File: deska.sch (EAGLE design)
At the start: 18 parts, among them Q1 BC547, Q2 BC547

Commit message: +
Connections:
- net +5V: now also TIN-2.KL, TOUT-2.KL, TUT-2.KL; no longer TIN-1.KL, TOUT-1.KL, TUT-1.KL
- net GND: now also TIN-1.KL, TOUT-1.KL, TUT-1.KL; no longer TIN-3.KL, TOUT-3.KL, TUT-3.KL
- net N$1: now also TIN-3.KL; no longer TIN-2.KL
- net N$19: now also TOUT-3.KL; no longer TOUT-2.KL
- net N$3: now also TUT-3.KL; no longer TUT-2.KL
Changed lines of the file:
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@@
 <wire x1="33.02" y1="60.96" x2="20.32" y2="60.96" width="0.1524" layer="91"/>
 <wire x1="20.32" y1="60.96" x2="12.7" y2="60.96" width="0.1524" layer="91"/>
-<wire x1="12.7" y1="91.44" x2="12.7" y2="60.96" width="0.1524" layer="91"/>
 <pinref part="R1" gate="G$1" pin="1"/>
+<wire x1="12.7" y1="88.9" x2="12.7" y2="60.96" width="0.1524" layer="91"/>
 <wire x1="20.32" y1="63.5" x2="20.32" y2="60.96" width="0.1524" layer="91"/>
 <junction x="20.32" y="60.96"/>
-<pinref part="TIN" gate="-2" pin="KL"/>
-<wire x1="-2.54" y1="91.44" x2="12.7" y2="91.44" width="0.1524" layer="91"/>
 <pinref part="WEMOS1" gate="D1" pin="D0"/>
 <wire x1="48.26" y1="66.04" x2="33.02" y2="66.04" width="0.1524" layer="91"/>
 <wire x1="33.02" y1="66.04" x2="33.02" y2="60.96" width="0.1524" layer="91"/>
+<pinref part="TIN" gate="-3" pin="KL"/>
+<wire x1="-2.54" y1="88.9" x2="12.7" y2="88.9" width="0.1524" layer="91"/>
 </segment>
 </net>
@@
 <segment>
 <wire x1="38.1" y1="53.34" x2="15.24" y2="53.34" width="0.1524" layer="91"/>
-<pinref part="TUT" gate="-2" pin="KL"/>
 <wire x1="15.24" y1="53.34" x2="7.62" y2="53.34" width="0.1524" layer="91"/>
-<wire x1="-2.54" y1="60.96" x2="7.62" y2="60.96" width="0.1524" layer="91"/>
-<wire x1="7.62" y1="60.96" x2="7.62" y2="53.34" width="0.1524" layer="91"/>
 <pinref part="R3" gate="G$1" pin="1"/>
+<wire x1="7.62" y1="58.42" x2="7.62" y2="53.34" width="0.1524" layer="91"/>
 <wire x1="15.24" y1="63.5" x2="15.24" y2="53.34" width="0.1524" layer="91"/>
 <junction x="15.24" y="53.34"/>
@@
 <wire x1="48.26" y1="60.96" x2="38.1" y2="60.96" width="0.1524" layer="91"/>
 <wire x1="38.1" y1="60.96" x2="38.1" y2="53.34" width="0.1524" layer="91"/>
+<pinref part="TUT" gate="-3" pin="KL"/>
+<wire x1="-2.54" y1="58.42" x2="7.62" y2="58.42" width="0.1524" layer="91"/>
 </segment>
 </net>
@@
 </segment>
 <segment>
-<wire x1="0" y1="73.66" x2="0" y2="58.42" width="0.1524" layer="91"/>
-<pinref part="TOUT" gate="-3" pin="KL"/>
-<wire x1="0" y1="58.42" x2="0" y2="53.34" width="0.1524" layer="91"/>
-<wire x1="-2.54" y1="73.66" x2="0" y2="73.66" width="0.1524" layer="91"/>
-<pinref part="GND5" gate="1" pin="GND"/>
-<pinref part="TUT" gate="-3" pin="KL"/>
-<wire x1="-2.54" y1="58.42" x2="0" y2="58.42" width="0.1524" layer="91"/>
-<junction x="0" y="58.42"/>
-<wire x1="0" y1="73.66" x2="0" y2="88.9" width="0.1524" layer="91"/>
-<junction x="0" y="73.66"/>
-<pinref part="TIN" gate="-3" pin="KL"/>
-<wire x1="0" y1="88.9" x2="-2.54" y2="88.9" width="0.1524" layer="91"/>
-</segment>
-<segment>
 <pinref part="NAPAJENI" gate="-2" pin="KL"/>
 <pinref part="GND6" gate="1" pin="GND"/>
+</segment>
+<segment>
+<pinref part="GND5" gate="1" pin="GND"/>
+<wire x1="0" y1="91.44" x2="0" y2="78.74" width="0.1524" layer="91"/>
+<wire x1="0" y1="78.74" x2="0" y2="76.2" width="0.1524" layer="91"/>
+<wire x1="0" y1="76.2" x2="0" y2="63.5" width="0.1524" layer="91"/>
+<wire x1="0" y1="63.5" x2="0" y2="60.96" width="0.1524" layer="91"/>
+<wire x1="0" y1="60.96" x2="0" y2="53.34" width="0.1524" layer="91"/>
+<pinref part="TIN" gate="-1" pin="KL"/>
+<wire x1="-2.54" y1="93.98" x2="0" y2="93.98" width="0.1524" layer="91"/>
+<wire x1="0" y1="93.98" x2="0" y2="91.44" width="0.1524" layer="91"/>
+<pinref part="TOUT" gate="-1" pin="KL"/>
+<wire x1="-2.54" y1="78.74" x2="0" y2="78.74" width="0.1524" layer="91"/>
+<junction x="0" y="78.74"/>
+<pinref part="TUT" gate="-1" pin="KL"/>
+<wire x1="-2.54" y1="63.5" x2="0" y2="63.5" width="0.1524" layer="91"/>
+<junction x="0" y="63.5"/>
 </segment>
 </net>
@@
 <junction x="20.32" y="73.66"/>
 <wire x1="25.4" y1="93.98" x2="25.4" y2="73.66" width="0.1524" layer="91"/>
-<pinref part="TIN" gate="-1" pin="KL"/>
-<wire x1="-2.54" y1="93.98" x2="2.54" y2="93.98" width="0.1524" layer="91"/>
-<wire x1="2.54" y1="63.5" x2="2.54" y2="78.74" width="0.1524" layer="91"/>
-<pinref part="TUT" gate="-1" pin="KL"/>
-<wire x1="2.54" y1="78.74" x2="2.54" y2="93.98" width="0.1524" layer="91"/>
-<wire x1="-2.54" y1="63.5" x2="2.54" y2="63.5" width="0.1524" layer="91"/>
 <wire x1="2.54" y1="93.98" x2="17.78" y2="93.98" width="0.1524" layer="91"/>
-<junction x="2.54" y="93.98"/>
-<pinref part="TOUT" gate="-1" pin="KL"/>
 <wire x1="17.78" y1="93.98" x2="25.4" y2="93.98" width="0.1524" layer="91"/>
-<wire x1="-2.54" y1="78.74" x2="2.54" y2="78.74" width="0.1524" layer="91"/>
-<junction x="2.54" y="78.74"/>
 <wire x1="20.32" y1="73.66" x2="25.4" y2="73.66" width="0.1524" layer="91"/>
 <pinref part="P+2" gate="1" pin="+5V"/>
 <wire x1="17.78" y1="99.06" x2="17.78" y2="93.98" width="0.1524" layer="91"/>
 <junction x="17.78" y="93.98"/>
+<pinref part="TIN" gate="-2" pin="KL"/>
+<wire x1="-2.54" y1="91.44" x2="2.54" y2="91.44" width="0.1524" layer="91"/>
+<wire x1="2.54" y1="91.44" x2="2.54" y2="93.98" width="0.1524" layer="91"/>
+<pinref part="TOUT" gate="-2" pin="KL"/>
+<wire x1="-2.54" y1="76.2" x2="2.54" y2="76.2" width="0.1524" layer="91"/>
+<wire x1="2.54" y1="76.2" x2="2.54" y2="91.44" width="0.1524" layer="91"/>
+<junction x="2.54" y="91.44"/>
+<pinref part="TUT" gate="-2" pin="KL"/>
+<wire x1="-2.54" y1="60.96" x2="2.54" y2="60.96" width="0.1524" layer="91"/>
+<wire x1="2.54" y1="60.96" x2="2.54" y2="76.2" width="0.1524" layer="91"/>
+<junction x="2.54" y="76.2"/>
 </segment>
 <segment>
@@
 <junction x="17.78" y="55.88"/>
 <wire x1="17.78" y1="55.88" x2="10.16" y2="55.88" width="0.1524" layer="91"/>
-<pinref part="TOUT" gate="-2" pin="KL"/>
-<wire x1="-2.54" y1="76.2" x2="10.16" y2="76.2" width="0.1524" layer="91"/>
-<wire x1="10.16" y1="76.2" x2="10.16" y2="55.88" width="0.1524" layer="91"/>
 <pinref part="WEMOS1" gate="D1" pin="D5"/>
+<wire x1="10.16" y1="73.66" x2="10.16" y2="55.88" width="0.1524" layer="91"/>
 <wire x1="48.26" y1="63.5" x2="35.56" y2="63.5" width="0.1524" layer="91"/>
 <wire x1="35.56" y1="63.5" x2="35.56" y2="55.88" width="0.1524" layer="91"/>
-</segment>
-</net>
+<pinref part="TOUT" gate="-3" pin="KL"/>
+<wire x1="-2.54" y1="73.66" x2="10.16" y2="73.66" width="0.1524" layer="91"/>
+</segment>
+</net>

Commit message: upravy desky
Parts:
- removed BUZZER, LED, NAPAJENI, RELAY: (no value), con-wago-508:W237-02P
- removed I2CDISP, I2CKEYB: (no value), con-wago-508:W237-04P
- removed Q1, Q2: BC547, transistor-npn:BC547
- removed R5, R6: 1k, rcl:R-EU_0207/7
- removed TIN, TOUT, TUT: (no value), con-wago-508:W237-3E
- added DS18B1, DS18B2, DS18B20, LED+RELAY: (no value), con-wago-508:W237-03P
- added PIR, SERIAL: (no value), con-amp-quick:M03
- added SL1: (no value), con-amp-quick:M04
- added SOURCE: (no value), con-wago-508:W237-02P
- R1, R3: device rcl:R-EU_0207/7 -> rcl:R-EU_0207/10
- R2: value 4k7 -> 220; device rcl:R-EU_0207/7 -> rcl:R-EU_0207/10
- R4: value 220 -> 4k7; device rcl:R-EU_0207/7 -> rcl:R-EU_0207/10
- WEMOS1: device wemos:WEMOS-D1-MINI -> esp8266modules:WEMOS-D1-MINI
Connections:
- removed net N$12: I2CDISP-3.KL, I2CKEYB-3.KL, WEMOS1.D4
- removed net N$14: Q2.C, RELAY-1.KL
- removed net N$15: BUZZER-1.KL, Q1.C
- removed net N$16: R6.2, WEMOS1.D2
- removed net N$19: R2.1, TOUT-3.KL, WEMOS1.D5
- new net N$2: SERIAL.3, WEMOS1.RX
- new net N$8: LED+RELAY-3.KL, R2.2
- new net N$9: DS18B20-2.KL, R1.2, WEMOS1.D7
- net +5V: now also DS18B1-3.KL, DS18B2-3.KL, DS18B20-3.KL, LED+RELAY-2.KL, PIR.3, R1.1, R3.1, R4.1, SL1.2, SOURCE-1.KL; no longer I2CDISP-2.KL, I2CKEYB-2.KL, LED-2.KL, NAPAJENI-1.KL, R1.2, R2.2, R3.2, RELAY-2.KL, TIN-2.KL, TOUT-2.KL, TUT-2.KL
- net GND: now also DS18B1-1.KL, DS18B2-1.KL, DS18B20-1.KL, PIR.1, SERIAL.1, SL1.1, SOURCE-2.KL; no longer BUZZER-2.KL, I2CDISP-1.KL, I2CKEYB-1.KL, NAPAJENI-2.KL, Q1.E, Q2.E, TIN-1.KL, TOUT-1.KL, TUT-1.KL
- net N$1: now also SERIAL.2, WEMOS1.TX; no longer R1.1, TIN-3.KL, WEMOS1.D0
- net N$11: now also DS18B2-2.KL, R4.2, WEMOS1.D5; no longer I2CDISP-4.KL, I2CKEYB-4.KL, WEMOS1.D3
- net N$13: now also DS18B1-2.KL, R3.2, WEMOS1.D6; no longer Q2.B, R5.2
- net N$3: now also SL1.4, WEMOS1.D1; no longer R3.1, TUT-3.KL, WEMOS1.D6
- net N$4: now also SL1.3, WEMOS1.D2; no longer R5.1, WEMOS1.D7
- net N$5: now also PIR.2, WEMOS1.D0; no longer R4.1, WEMOS1.D8
- net N$6: now also R2.1, WEMOS1.D4; no longer LED-1.KL, R4.2
- net N$7: now also LED+RELAY-1.KL, WEMOS1.D3; no longer Q1.B, R6.1
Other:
- moved on the sheet: R1, R2, R3, R4, WEMOS1

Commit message: +
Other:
- moved on the sheet: R4
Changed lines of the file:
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@@
 <attribute name="VALUE" x="16.51" y="64.262" size="1.778" layer="96" rot="R180"/>
 </instance>
-<instance part="R4" gate="G$1" x="-12.7" y="63.5" smashed="yes" rot="R180">
-<attribute name="NAME" x="-8.89" y="62.0014" size="1.778" layer="95" rot="R180"/>
-<attribute name="VALUE" x="-8.89" y="66.802" size="1.778" layer="96" rot="R180"/>
+<instance part="R4" gate="G$1" x="-10.16" y="63.5" smashed="yes" rot="R180">
+<attribute name="NAME" x="-6.35" y="62.0014" size="1.778" layer="95" rot="R180"/>
+<attribute name="VALUE" x="-6.35" y="66.802" size="1.778" layer="96" rot="R180"/>
 </instance>
 <instance part="SOURCE" gate="-1" x="17.78" y="15.24" smashed="yes">
@@
 <pinref part="DS18B20" gate="-1" pin="KL"/>
 <pinref part="GND4" gate="1" pin="GND"/>
+<pinref part="DS18B1" gate="-1" pin="KL"/>
+<wire x1="5.08" y1="50.8" x2="27.94" y2="50.8" width="0.1524" layer="91"/>
+<junction x="27.94" y="50.8"/>
 <pinref part="DS18B2" gate="-1" pin="KL"/>
-<pinref part="DS18B1" gate="-1" pin="KL"/>
 <wire x1="-17.78" y1="50.8" x2="5.08" y2="50.8" width="0.1524" layer="91"/>
-<wire x1="5.08" y1="50.8" x2="27.94" y2="50.8" width="0.1524" layer="91"/>
 <junction x="5.08" y="50.8"/>
-<junction x="27.94" y="50.8"/>
 </segment>
 <segment>
@@
 <pinref part="R3" gate="G$1" pin="1"/>
 <wire x1="17.78" y1="45.72" x2="27.94" y2="45.72" width="0.1524" layer="91"/>
-<wire x1="-7.62" y1="63.5" x2="17.78" y2="63.5" width="0.1524" layer="91"/>
+<wire x1="-5.08" y1="63.5" x2="17.78" y2="63.5" width="0.1524" layer="91"/>
 <wire x1="17.78" y1="63.5" x2="17.78" y2="60.96" width="0.1524" layer="91"/>
 <wire x1="17.78" y1="60.96" x2="17.78" y2="45.72" width="0.1524" layer="91"/>
@@
 <wire x1="40.64" y1="58.42" x2="0" y2="58.42" width="0.1524" layer="91"/>
 <wire x1="0" y1="58.42" x2="0" y2="55.88" width="0.1524" layer="91"/>
+<pinref part="R4" gate="G$1" pin="2"/>
+<wire x1="-15.24" y1="55.88" x2="-15.24" y2="63.5" width="0.1524" layer="91"/>
+<wire x1="0" y1="55.88" x2="-15.24" y2="55.88" width="0.1524" layer="91"/>
 <pinref part="DS18B2" gate="-2" pin="KL"/>
-<pinref part="R4" gate="G$1" pin="2"/>
-<wire x1="-17.78" y1="48.26" x2="-17.78" y2="55.88" width="0.1524" layer="91"/>
-<wire x1="-17.78" y1="55.88" x2="-17.78" y2="63.5" width="0.1524" layer="91"/>
-<wire x1="0" y1="55.88" x2="-17.78" y2="55.88" width="0.1524" layer="91"/>
-<junction x="-17.78" y="55.88"/>
+<wire x1="-17.78" y1="48.26" x2="-15.24" y2="48.26" width="0.1524" layer="91"/>
+<wire x1="-15.24" y1="48.26" x2="-15.24" y2="55.88" width="0.1524" layer="91"/>
+<junction x="-15.24" y="55.88"/>
 </segment>
 </net>
@@
 </sheet>
 </sheets>
+<errors>
+</errors>
 </schematic>
 </drawing>

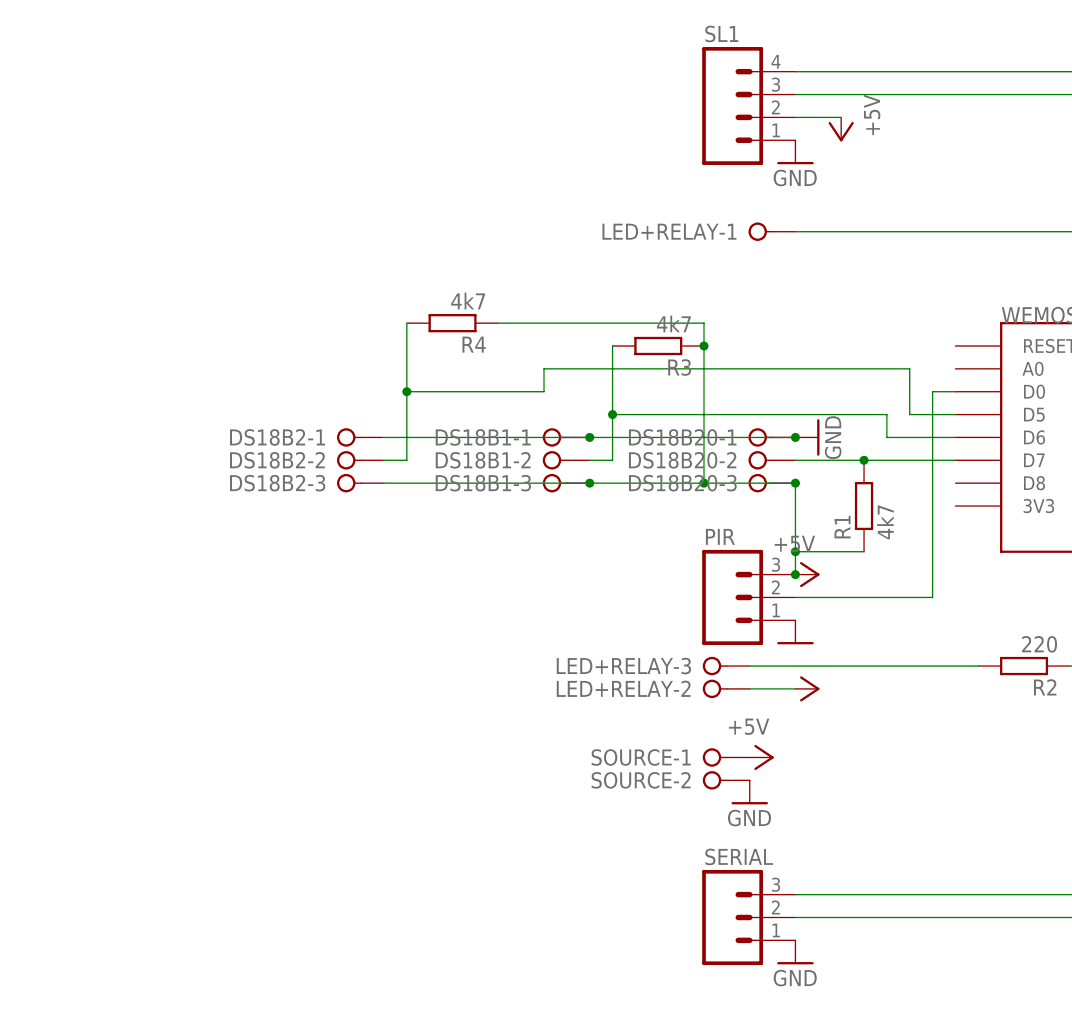
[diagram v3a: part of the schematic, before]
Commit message: změna na JST XH konektory
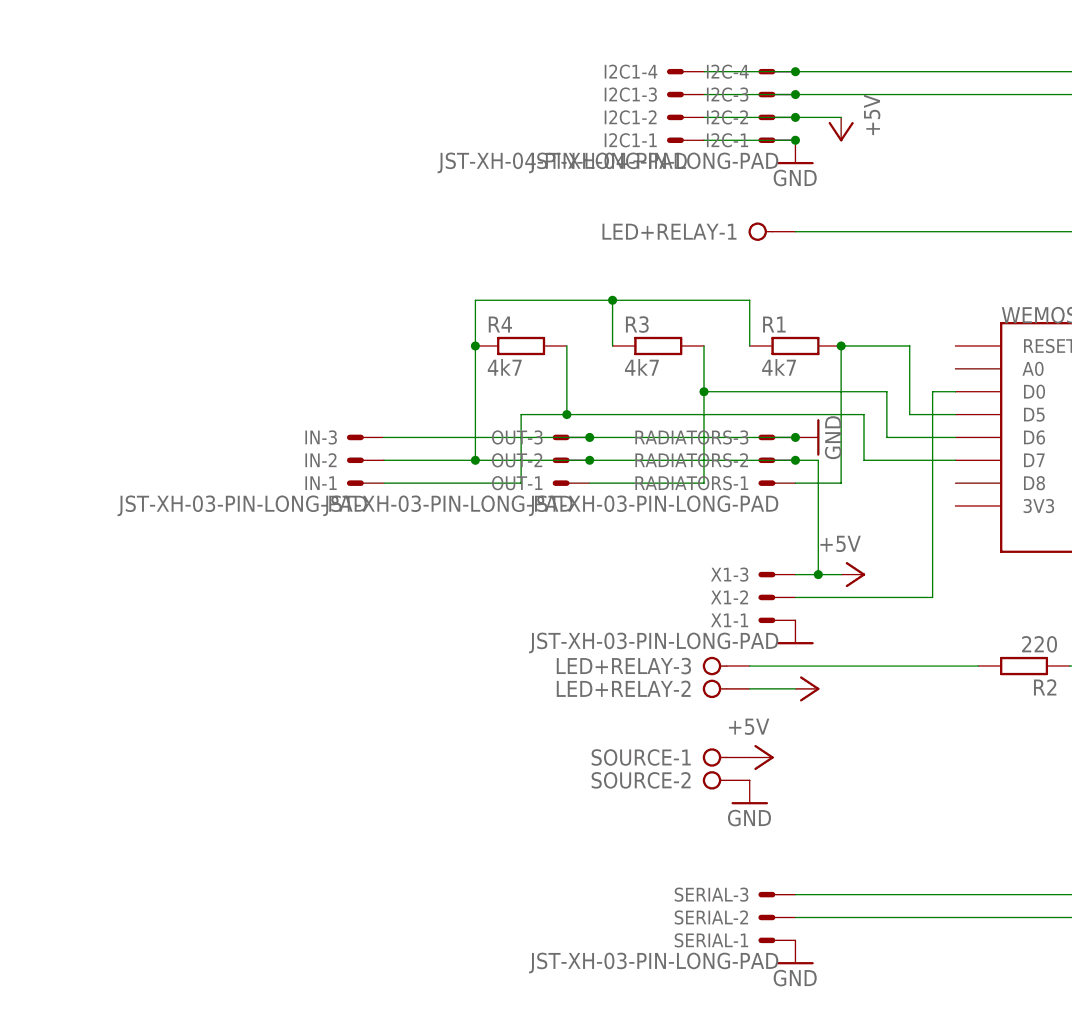
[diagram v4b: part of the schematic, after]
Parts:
- removed DS18B1, DS18B2, DS18B20: (no value), con-wago-508:W237-03P
- removed PIR: (no value), con-amp-quick:M03
- removed SL1: (no value), con-amp-quick:M04
- added I2C, I2C1: JST-XH-04-PIN-LONG-PAD, Rembrandt Electronics - JST XH Connectors v1-0:JST-XH-04-PIN-LONG-PAD
- added IN, OUT, RADIATORS, X1: JST-XH-03-PIN-LONG-PAD, Rembrandt Electronics - JST XH Connectors v1-0:JST-XH-03-PIN-LONG-PAD
- SERIAL: value (none) -> JST-XH-03-PIN-LONG-PAD; device con-amp-quick:M03 -> Rembrandt Electronics - JST XH Connectors v1-0:JST-XH-03-PIN-LONG-PAD
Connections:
- net +5V: now also I2C-2.S, I2C1-2.S, IN-2.S, OUT-2.S, RADIATORS-2.S, X1-3.S; no longer DS18B1-3.KL, DS18B2-3.KL, DS18B20-3.KL, PIR.3, SL1.2
- net GND: now also I2C-1.S, I2C1-1.S, IN-3.S, OUT-3.S, RADIATORS-3.S, SERIAL-1.S, X1-1.S; no longer DS18B1-1.KL, DS18B2-1.KL, DS18B20-1.KL, PIR.1, SERIAL.1, SL1.1
- net N$1: now also SERIAL-2.S; no longer SERIAL.2
- net N$11: now also R1.2, RADIATORS-1.S; no longer DS18B2-2.KL, R4.2
- net N$13: now also OUT-1.S; no longer DS18B1-2.KL
- net N$2: now also SERIAL-3.S; no longer SERIAL.3
- net N$3: now also I2C-4.S, I2C1-4.S; no longer SL1.4
- net N$4: now also I2C-3.S, I2C1-3.S; no longer SL1.3
- net N$5: now also X1-2.S; no longer PIR.2
- net N$9: now also IN-1.S, R4.2; no longer DS18B20-2.KL, R1.2
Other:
- moved on the sheet: R1, R3, R4
